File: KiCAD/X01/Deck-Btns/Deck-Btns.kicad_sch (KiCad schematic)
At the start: 45 parts, among them J1 Conn_01x05, J2 Conn_01x05, SW1 SW_Push_LED, SW10 SW_Push_LED, SW2 SW_Push_LED, SW3 SW_Push_LED, SW4 SW_Push_LED, SW5 SW_Push_LED, SW6 SW_Push_LED, SW7 SW_Push_LED, SW8 SW_Push_LED, SW9 SW_Push_LED, U1 CD74HC4067M, U2 74HC595, U3 74HC595

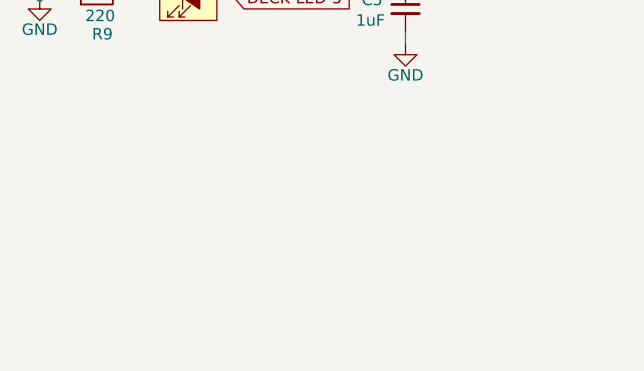
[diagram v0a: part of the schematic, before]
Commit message: deck btns fixes
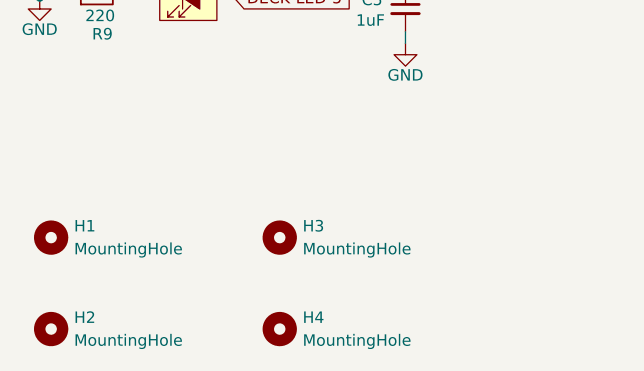
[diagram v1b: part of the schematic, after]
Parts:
- added H1, H2, H3, H4: MountingHole, MountingHole:MountingHole_3.2mm_M3, symbol Mechanical:MountingHole

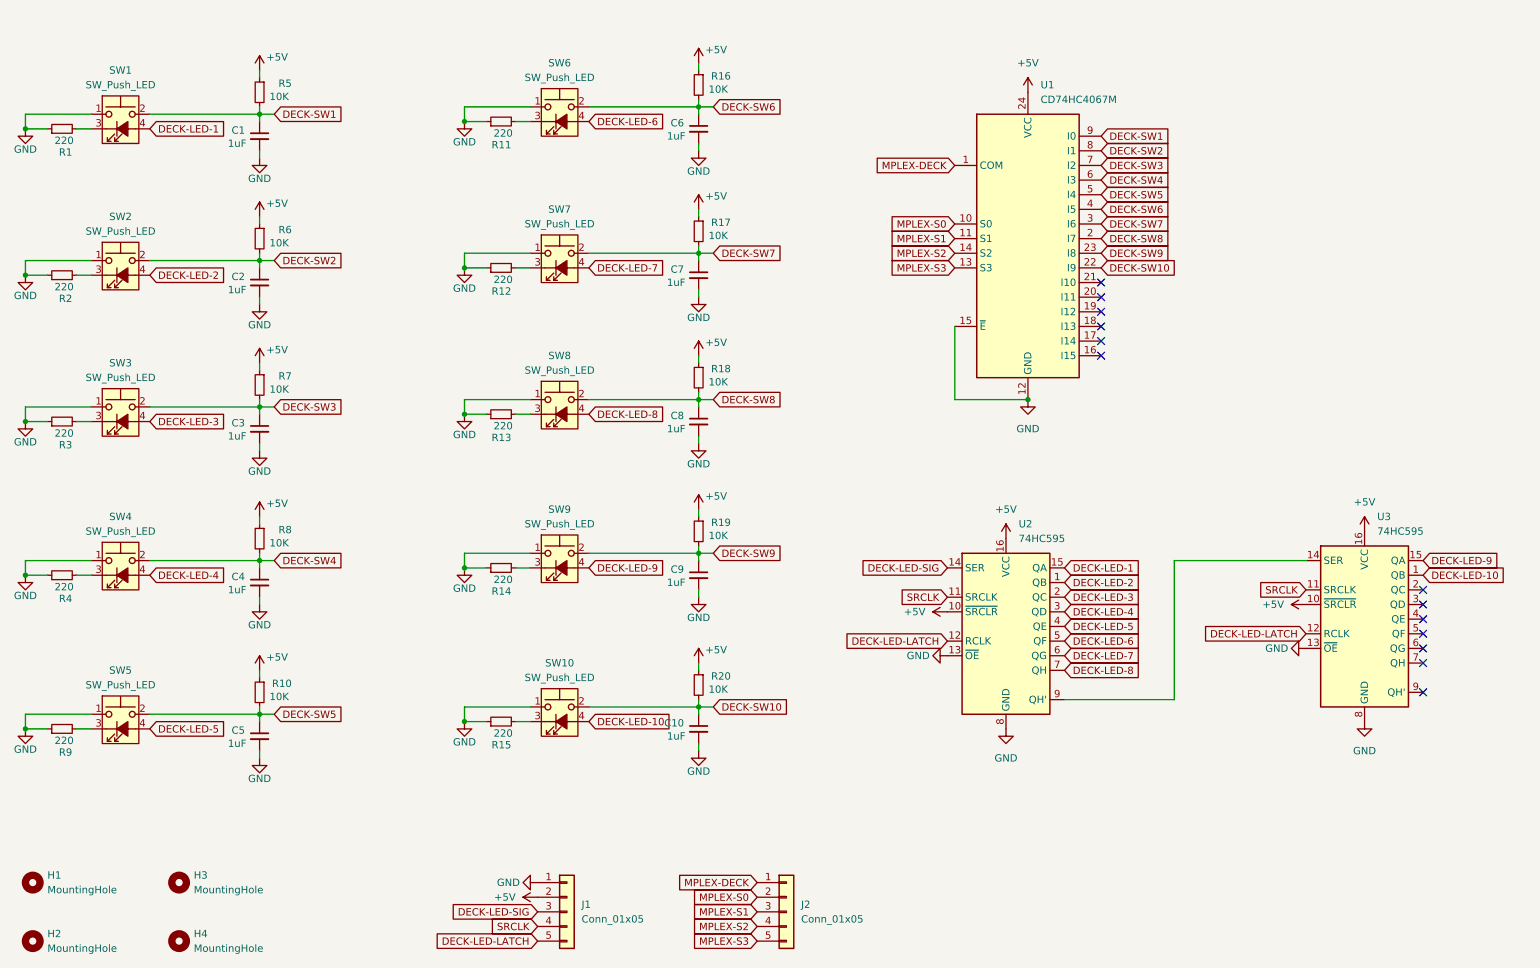
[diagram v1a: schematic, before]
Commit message: ht16k33 deck btns
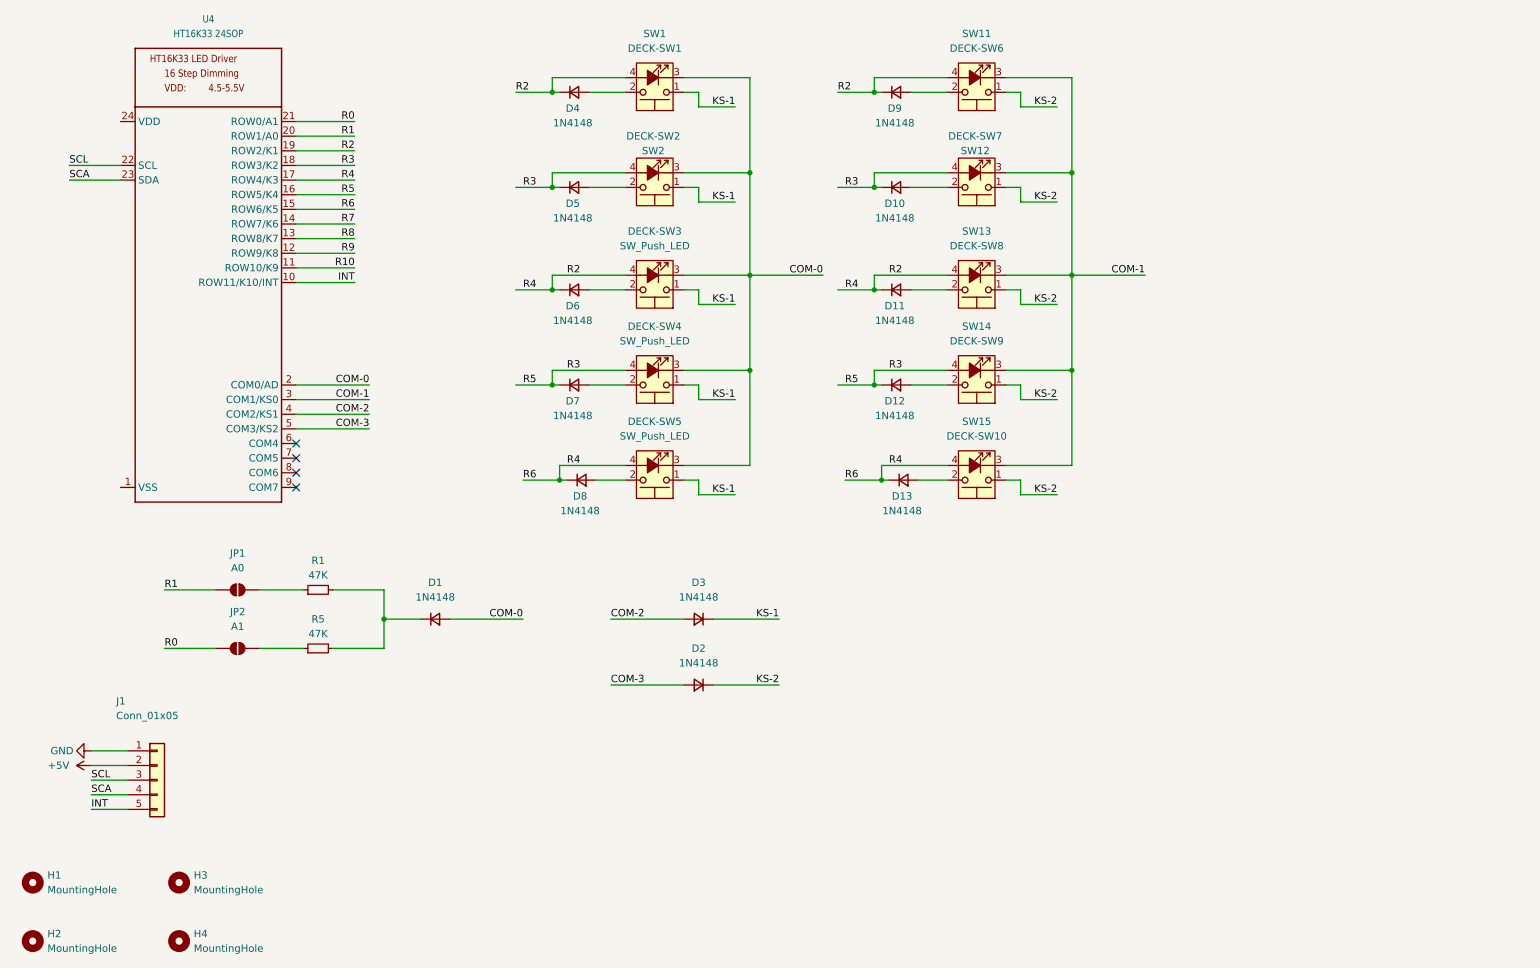
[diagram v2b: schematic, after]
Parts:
- removed C1, C10, C2, C3, C4, C5, C6, C7, C8, C9: 1uF, Capacitor_SMD:C_1206_3216Metric_Pad1.33x1.80mm_HandSolder, symbol Device:C_Small
- removed J2: Conn_01x05, Connector_PinHeader_2.54mm:PinHeader_1x05_P2.54mm_Vertical, symbol Connector_Generic:Conn_01x05
- removed R10, R16, R17, R18, R19, R20, R6, R7, R8: 10K, PCM_Resistor_SMD_AKL:R_1206_3216Metric_Pad1.30x1.75mm_HandSolder, symbol Device:R_Small
- removed R11, R12, R13, R14, R15, R2, R3, R4, R9: 220, PCM_Resistor_SMD_AKL:R_1206_3216Metric_Pad1.30x1.75mm_HandSolder, symbol Device:R_Small
- removed SW10, SW6, SW7, SW8, SW9: SW_Push_LED, led-switch:SW_PUSH_6mm_LED, symbol Switch:SW_Push_LED
- removed U1: CD74HC4067M, Package_SO:SOIC-24W_7.5x15.4mm_P1.27mm, symbol 74xx:CD74HC4067M
- removed U2, U3: 74HC595, Package_SO:SOIC-16_3.9x9.9mm_P1.27mm, symbol 74xx:74HC595
- added D1, D10, D11, D12, D13, D2, D3, D4, D5, D6, D7, D8, D9: 1N4148, symbol Device:D_Small
- added JP1: A0, Jumper:SolderJumper-2_P1.3mm_Open_RoundedPad1.0x1.5mm, symbol Jumper:SolderJumper_2_Open
- added JP2: A1, Jumper:SolderJumper-2_P1.3mm_Open_RoundedPad1.0x1.5mm, symbol Jumper:SolderJumper_2_Open
- added SW11: DECK-SW6, led-switch:SW_PUSH_6mm_LED, symbol Switch:SW_Push_LED
- added SW12: DECK-SW7, led-switch:SW_PUSH_6mm_LED, symbol Switch:SW_Push_LED
- added SW13: DECK-SW8, led-switch:SW_PUSH_6mm_LED, symbol Switch:SW_Push_LED
- added SW14: DECK-SW9, led-switch:SW_PUSH_6mm_LED, symbol Switch:SW_Push_LED
- added SW15: DECK-SW10, led-switch:SW_PUSH_6mm_LED, symbol Switch:SW_Push_LED
- added U4: HT16K33 24SOP, Package_SO:SSOP-24_5.3x8.2mm_P0.65mm, symbol ht16k33_sop28:HT16K33_SOP24
- R1: value 220 -> 47K; footprint PCM_Resistor_SMD_AKL:R_1206_3216Metric_Pad1.30x1.75mm_HandSolder -> (none)
- R5: value 10K -> 47K; footprint PCM_Resistor_SMD_AKL:R_1206_3216Metric_Pad1.30x1.75mm_HandSolder -> (none)
- SW1: value SW_Push_LED -> DECK-SW1
- SW2: value SW_Push_LED -> DECK-SW2
- renumbered SW3 to DECK-SW3, SW4 to DECK-SW4, SW5 to DECK-SW5
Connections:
- net DECK-LED-3 is gone; now on net R2: DECK-SW3.4 (A)
- net DECK-LED-4 is gone; now on net R3: DECK-SW4.4 (A)
- net DECK-LED-5 is gone; now on net R2: DECK-SW5.4 (A)
- net +5V: no longer R5.1
- net GND: no longer DECK-SW3.1, DECK-SW4.1, DECK-SW5.1, R1.1, SW1.1, SW2.1
- net COM-0: now reaches DECK-SW3.3 (K)
- net COM-0: now also DECK-SW4.3 (K), DECK-SW5.3 (K), SW1.3 (K), SW2.3 (K), D1.2 (A), U4.2 (COM0/AD)
- net at R1.2: now also R5.2, D1.1 (K); no longer SW1.3 (K)
- net DECK-LED-1 renamed R2
- net R2: now also D11.1 (K), D13.1 (K), D4.1 (K), D6.1 (K), D8.1 (K), D9.1 (K), SW11.4 (A), SW13.4 (A), SW15.4 (A), U4.15 (ROW6/K5), U4.17 (ROW4/K3), U4.19 (ROW2/K1)
- net DECK-LED-2 renamed R3
- net R3: now also D10.1 (K), D12.1 (K), D5.1 (K), D7.1 (K), SW12.4 (A), SW14.4 (A), U4.16 (ROW5/K4), U4.18 (ROW3/K2)
- net DECK-LED-LATCH renamed INT
- net INT: now also U4.10 (ROW11/K10/INT)
- net DECK-LED-SIG renamed SCL
- net SCL: now also U4.22 (SCL)
- net DECK-SW1: no longer names the net of SW1.2
- net DECK-SW1: now also D4.2 (A); no longer R5.2
- net DECK-SW2: no longer names the net of SW2.2
- net DECK-SW2: now also D5.2 (A)
- net DECK-SW3: no longer names the net of DECK-SW3.2
- net DECK-SW3: now also D6.2 (A)
- net DECK-SW4: no longer names the net of DECK-SW4.2
- net DECK-SW4: now also D7.2 (A)
- net DECK-SW5: no longer names the net of DECK-SW5.2
- net DECK-SW5: now also D8.2 (A)
- net SRCLK renamed SCA
- net SCA: now also U4.23 (SDA)
- new net: D12.2 (A), SW14.2
- new net: D9.2 (A), SW11.2
- new net: JP1.2 (B), R1.1
- new net: JP2.2 (B), R5.1
- new net: D13.2 (A), SW15.2
- new net: D11.2 (A), SW13.2
- new net: D10.2 (A), SW12.2
- new net COM-1: SW11.3 (K), SW12.3 (K), SW13.3 (K), SW14.3 (K), SW15.3 (K), U4.3 (COM1/KS0)
- new net COM-2: D3.2 (A), U4.4 (COM2/KS1)
- new net COM-3: D2.2 (A), U4.5 (COM3/KS2)
- new net KS-1: D3.1 (K), DECK-SW3.1, DECK-SW4.1, DECK-SW5.1, SW1.1, SW2.1
- new net KS-2: D2.1 (K), SW11.1, SW12.1, SW13.1, SW14.1, SW15.1
- new net R0: JP2.1 (A), U4.21 (ROW0/A1)
- new net R1: JP1.1 (A), U4.20 (ROW1/A0)
- new net R10: U4.11 (ROW10/K9)
- new net R7: U4.14 (ROW7/K6)
- new net R8: U4.13 (ROW8/K7)
- new net R9: U4.12 (ROW9/K8)
- no-connect marks 13 -> 4
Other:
- moved on the sheet: DECK-SW3, DECK-SW4, DECK-SW5, J1, SW1, SW2

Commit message: dck btns
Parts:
- D1, D10, D11, D12, D13, D9: footprint (none) -> Diode_SMD:D_SOD-123
- D2: renamed from D4; footprint (none) -> Diode_SMD:D_SOD-123
- D3: renamed from D5; footprint (none) -> Diode_SMD:D_SOD-123
- D4: renamed from D6; footprint (none) -> Diode_SMD:D_SOD-123
- D5: renamed from D7; footprint (none) -> Diode_SMD:D_SOD-123
- D6: renamed from D8; footprint (none) -> Diode_SMD:D_SOD-123
- D7: renamed from D3; footprint (none) -> Diode_SMD:D_SOD-123
- D8: renamed from D2; footprint (none) -> Diode_SMD:D_SOD-123
- R1: footprint (none) -> Resistor_SMD:R_0805_2012Metric_Pad1.20x1.40mm_HandSolder
- R2: renamed from R5; footprint (none) -> Resistor_SMD:R_0805_2012Metric_Pad1.20x1.40mm_HandSolder
- SW1, SW2: footprint led-switch:SW_PUSH_6mm_LED -> led-sw:led switch
- SW10: renamed from SW15; footprint led-switch:SW_PUSH_6mm_LED -> led-sw:led switch
- SW3: renamed from DECK-SW3; value SW_Push_LED -> DECK-SW3; footprint led-switch:SW_PUSH_6mm_LED -> led-sw:led switch
- SW4: renamed from DECK-SW4; value SW_Push_LED -> DECK-SW4; footprint led-switch:SW_PUSH_6mm_LED -> led-sw:led switch
- SW5: renamed from DECK-SW5; value SW_Push_LED -> DECK-SW5; footprint led-switch:SW_PUSH_6mm_LED -> led-sw:led switch
- SW6: renamed from SW11; footprint led-switch:SW_PUSH_6mm_LED -> led-sw:led switch
- SW7: renamed from SW12; footprint led-switch:SW_PUSH_6mm_LED -> led-sw:led switch
- SW8: renamed from SW13; footprint led-switch:SW_PUSH_6mm_LED -> led-sw:led switch
- SW9: renamed from SW14; footprint led-switch:SW_PUSH_6mm_LED -> led-sw:led switch
- renumbered U4 to U1
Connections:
- net +5V is gone; now on net VCC: J1.2 (Pin_2)
- net GND: now also U1.1 (VSS)
- net R2: no longer D11.1 (K), D13.1 (K), D4.1 (K), D6.1 (K), SW10.4 (A), SW3.4 (A), SW5.4 (A), SW8.4 (A), U1.15 (ROW6/K5), U1.17 (ROW4/K3)
- net R3: no longer D12.1 (K), D5.1 (K), SW4.4 (A), SW9.4 (A), U1.16 (ROW5/K4)
- net VCC: now reaches U1.24 (VDD)
- net R10: no longer names the net of U1.11 (ROW10/K9)
- net R7: no longer names the net of U1.14 (ROW7/K6)
- net R8: no longer names the net of U1.13 (ROW8/K7)
- net R9: no longer names the net of U1.12 (ROW9/K8)
- new net R4: D11.1 (K), D4.1 (K), SW3.4 (A), SW8.4 (A), U1.17 (ROW4/K3)
- new net R5: D12.1 (K), D5.1 (K), SW4.4 (A), SW9.4 (A), U1.16 (ROW5/K4)
- new net R6: D13.1 (K), D6.1 (K), SW10.4 (A), SW5.4 (A), U1.15 (ROW6/K5)
- no-connect marks 4 -> 8
